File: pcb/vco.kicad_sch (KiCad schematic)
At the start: 20 parts, among them J5 AudioJack2, Q1 BC558, Q2 BC548, U1 40106, U2 TL072

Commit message: update vca
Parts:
- removed D1: 1N4148WT, Diode_SMD:D_SOD-523, symbol Diode:1N4148WT
- removed Q1: BC558, symbol Simulation_SPICE:PNP
- removed Q2: BC548, symbol Simulation_SPICE:NPN
- added D11: 1N4148, Diode_THT:D_DO-35_SOD27_P7.62mm_Horizontal, symbol Diode:1N4148
- added Q2: BC558, Package_TO_SOT_THT:TO-92_Inline, symbol Transistor_BJT:BC558
- added Q5: BC548, Package_TO_SOT_THT:TO-92_Inline, symbol Transistor_BJT:BC548
- C1, C12, C13, C14, C2: footprint (none) -> Capacitor_THT:C_Disc_D6.0mm_W2.5mm_P5.00mm
- J5: footprint (none) -> Connector_Audio:Jack_3.5mm_CUI_SJ1-3513N_Horizontal
- R1, R2, R3, R4, R5, R6, R7: footprint (none) -> Resistor_THT:R_Axial_DIN0207_L6.3mm_D2.5mm_P10.16mm_Horizontal
- RV1: footprint (none) -> Potentiometer_THT:Potentiometer_Bourns_PTV09A-1_Single_Vertical
- RV2: footprint (none) -> Potentiometer_THT:Potentiometer_Bourns_3296W_Vertical
- U1: footprint (none) -> Package_DIP:DIP-14_W7.62mm
- U2: footprint (none) -> Package_DIP:DIP-8_W7.62mm
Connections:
- net -2V5: now also Q2.1 (C)
- net GND: now also Q5.3 (E)
- net at C1.1, U1.1, U2.3 (+): now also D11.1 (K), Q5.1 (C)
- net at U1.2: now also D11.2 (A)
- net at R1.2, R2.2, R3.1: now also Q2.2 (B)
- net at R4.2: now also Q2.3 (E), Q5.2 (B)

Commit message: Update rails, start to clean
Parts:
- added JP1: SolderJumper_3_Bridged12, symbol Jumper:SolderJumper_3_Bridged12
- R3: value 1.5k -> 2k
- RV2: now not fitted
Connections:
- net GND: now also JP1.1 (A)
- net at RV2.1: now also JP1.3 (B); no longer R3.2
- net +2V5 renamed +9V
- net -2V5 renamed -9V
- new net: JP1.2 (C), R3.2
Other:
- note added: "1.5k if RV2 installed"
- note added: "TODO: Replace with 2k? Only need pot for CV tracking"
- note removed: "TODO: Need for demo?"

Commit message: Didn't save
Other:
- note removed: "TODO: Replace with 2k? Only need pot for CV tracking"
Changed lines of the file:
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@@
-		)
-	)
-	(text "TODO: Replace with 2k?\nOnly need pot for CV tracking"
-		(exclude_from_sim no)
-		(at 44.958 124.714 0)
-		(effects
-			(font
-				(size 1.27 1.27)
-			)
 		)
 	)

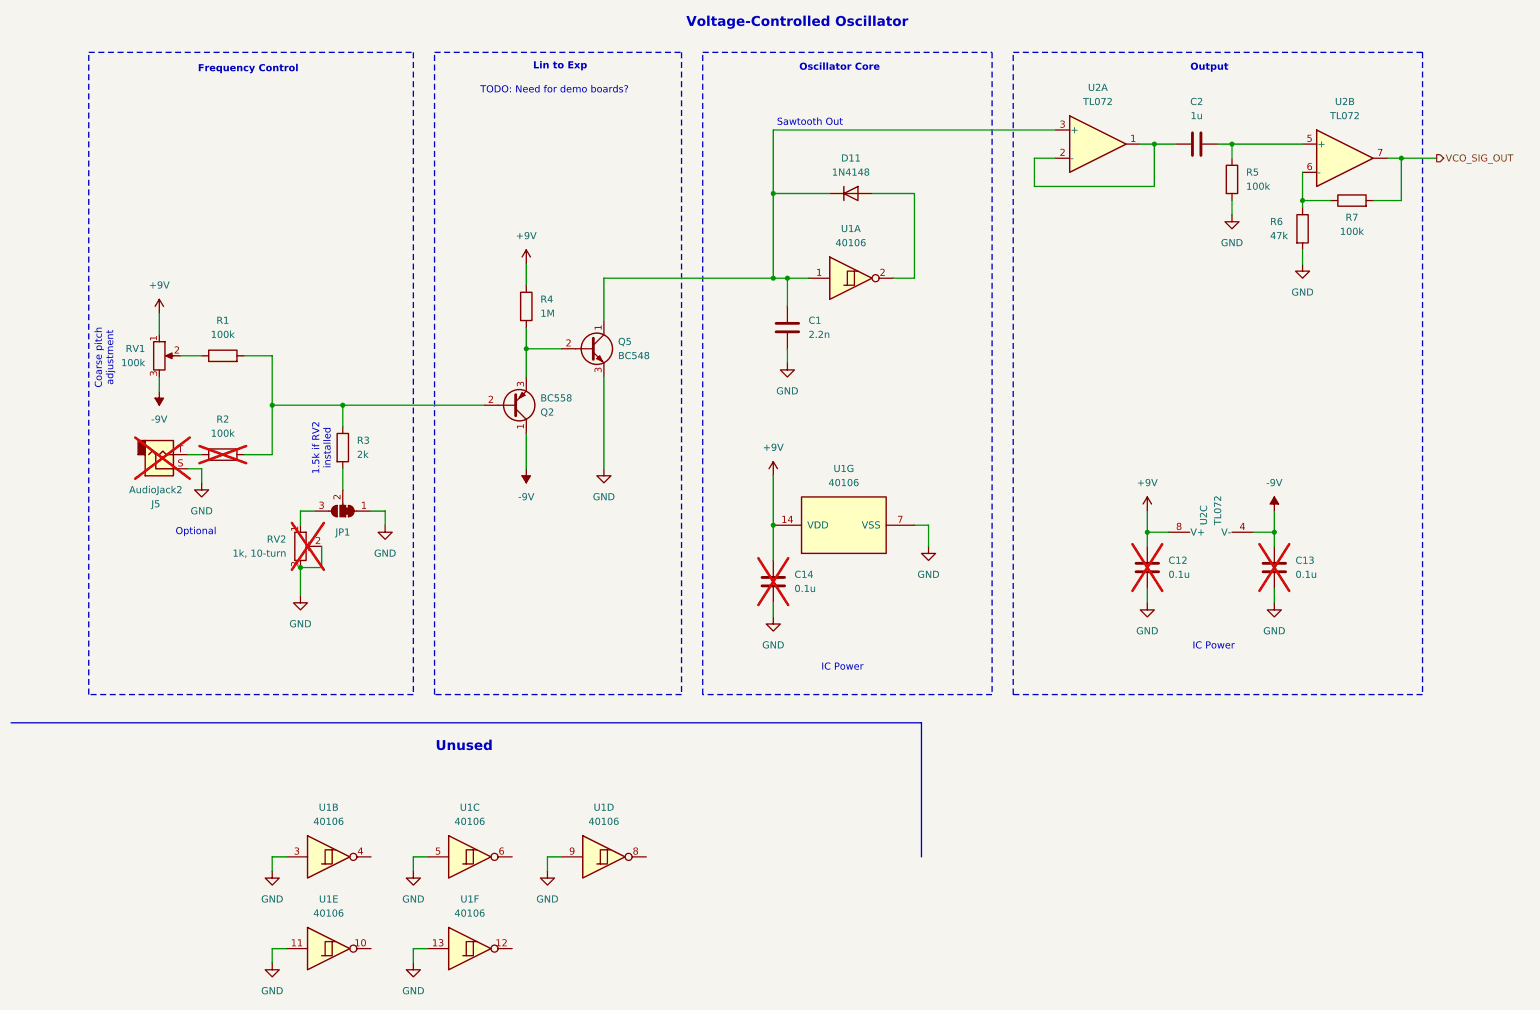
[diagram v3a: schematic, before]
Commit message: Fix some labeling and DNP statues
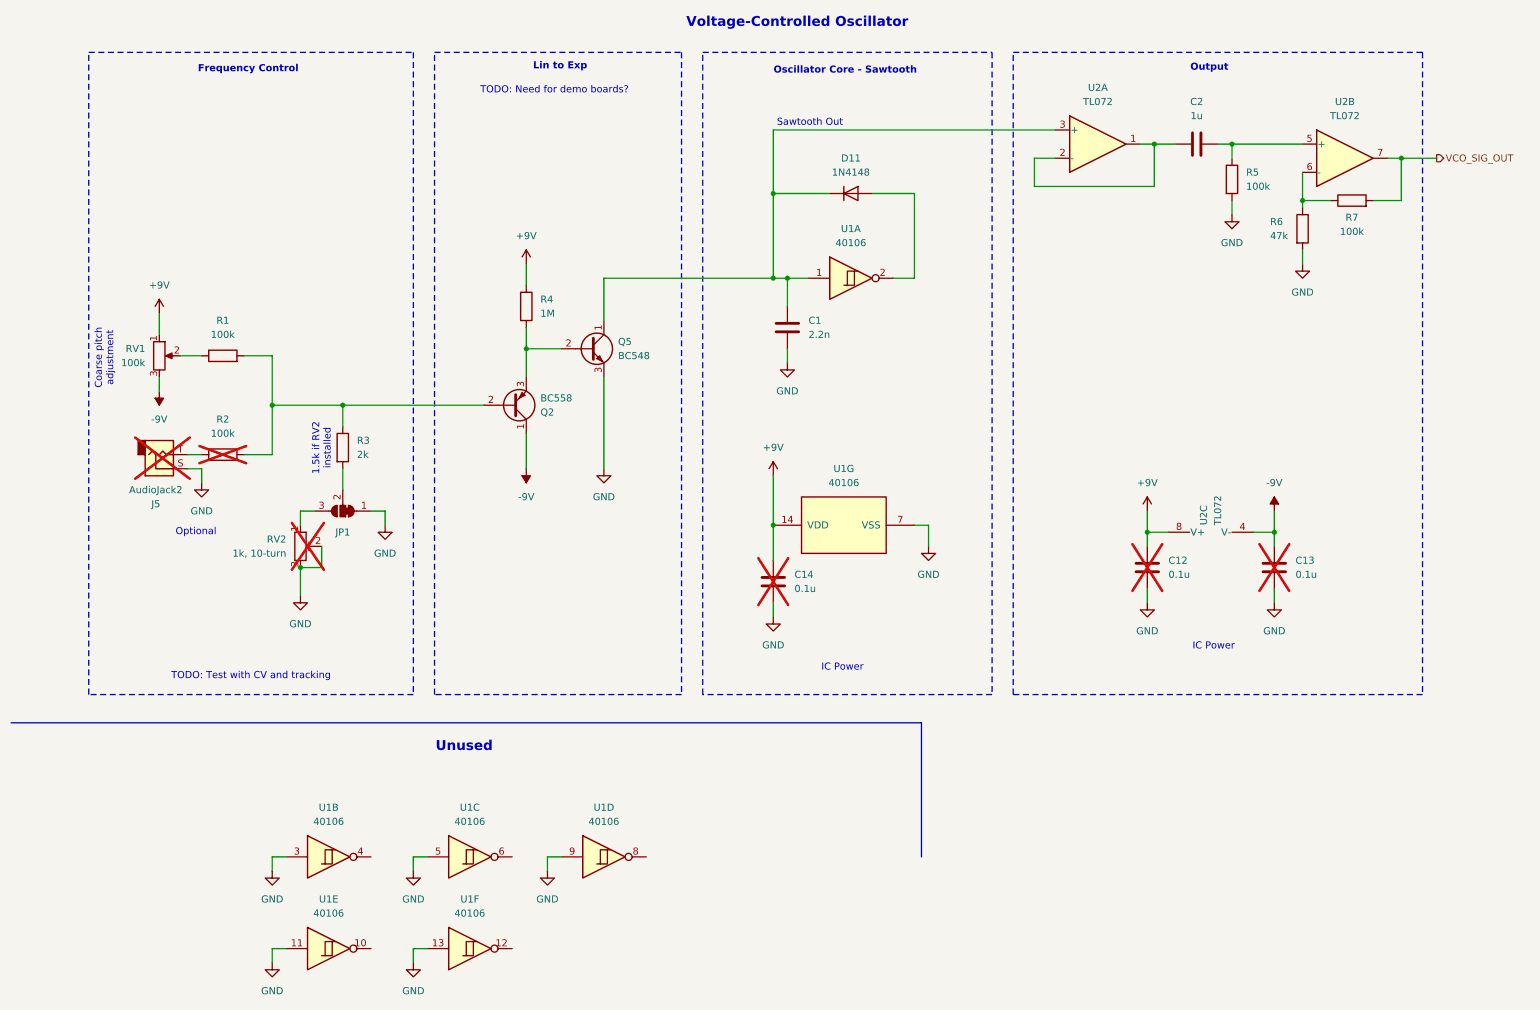
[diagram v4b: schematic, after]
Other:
- note added: "Oscillator Core - Sawtooth"
- note added: "TODO: Test with CV and tracking"
- note removed: "Oscillator Core"
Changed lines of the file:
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@@
 		)
 	)
-	(text "Oscillator Core\n"
+	(text "Oscillator Core - Sawtooth\n"
 		(exclude_from_sim no)
-		(at 161.798 24.384 0)
+		(at 162.814 24.892 0)
 		(effects
 			(font
@@
 			)
 		)
+	)
+	(text "TODO: Test with CV and tracking"
+		(exclude_from_sim no)
+		(at 55.88 133.858 0)
+		(effects
+			(font
+				(size 1.27 1.27)
+				(color 255 0 252 1)
+			)
+		)
